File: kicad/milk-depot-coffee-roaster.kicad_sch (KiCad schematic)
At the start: 8 parts, among them J1 BT Thermocouple (35mm/2.5mm), J2 ET Thermocouple (50mm/3.0mm), J3 OLED 1.3in IIC, U1 MAX31855KASA, U2 MAX31855KASA

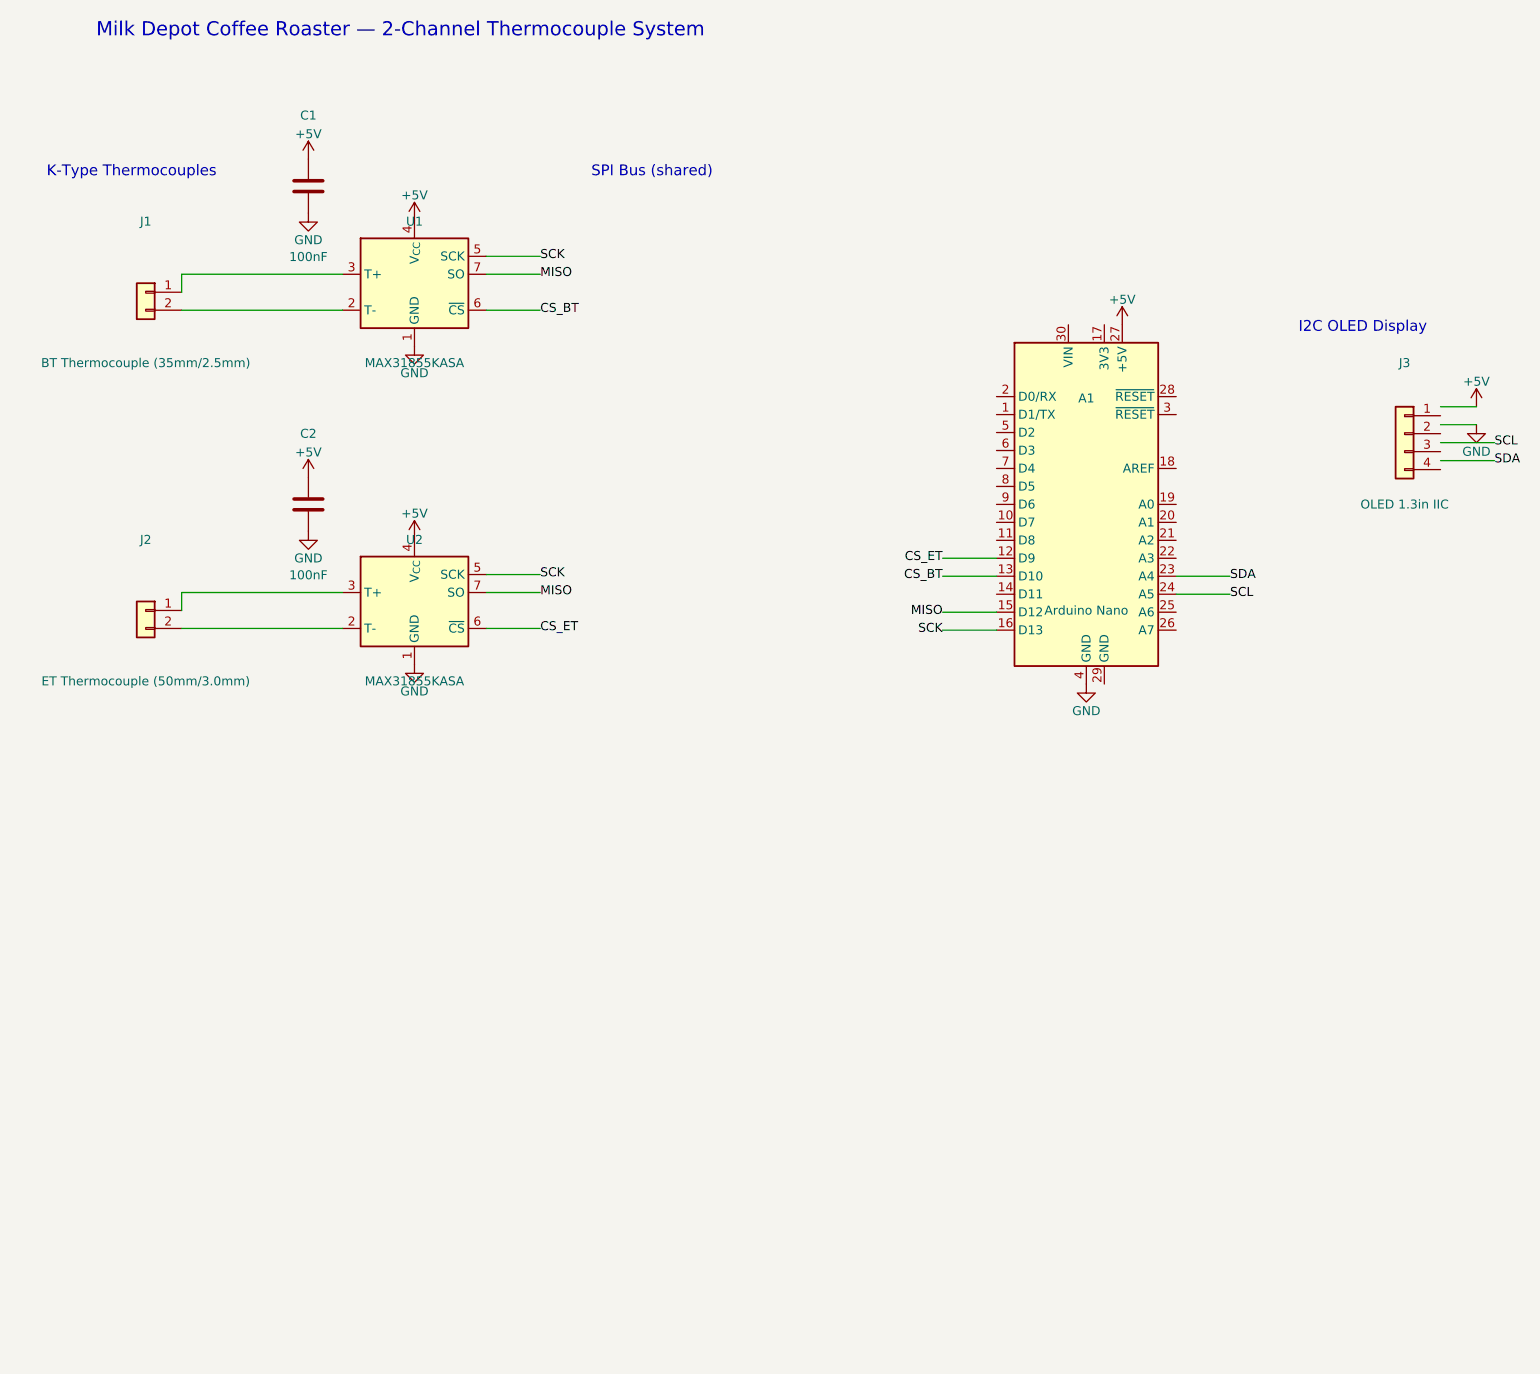
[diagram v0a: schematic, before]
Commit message: Scaffold new KiCad 10 project for ESP32 redesign
- Archive old Arduino Nano schematic to kicad/archive/v1-nano/
- New project with JLCPCB-compatible design rules (2-layer, A3 schematic)
- Place ESP32-WROOM-32E, 2× MAX31855KASA, 2× BSS138 symbols (validated against datasheets)
- Set up project-local symbol/footprint libraries and BOM fields (MPN, DigiKey_PN)
- Add component datasheets (ESP32, MAX31855, BSS138, LCD)
- Update .gitignore for KiCad 10 patterns
- Update RESUME.md and STATUS.md with procurement and schematic progress

Co-Authored-By: Claude Opus 4.6 (1M context) <noreply@anthropic.com>
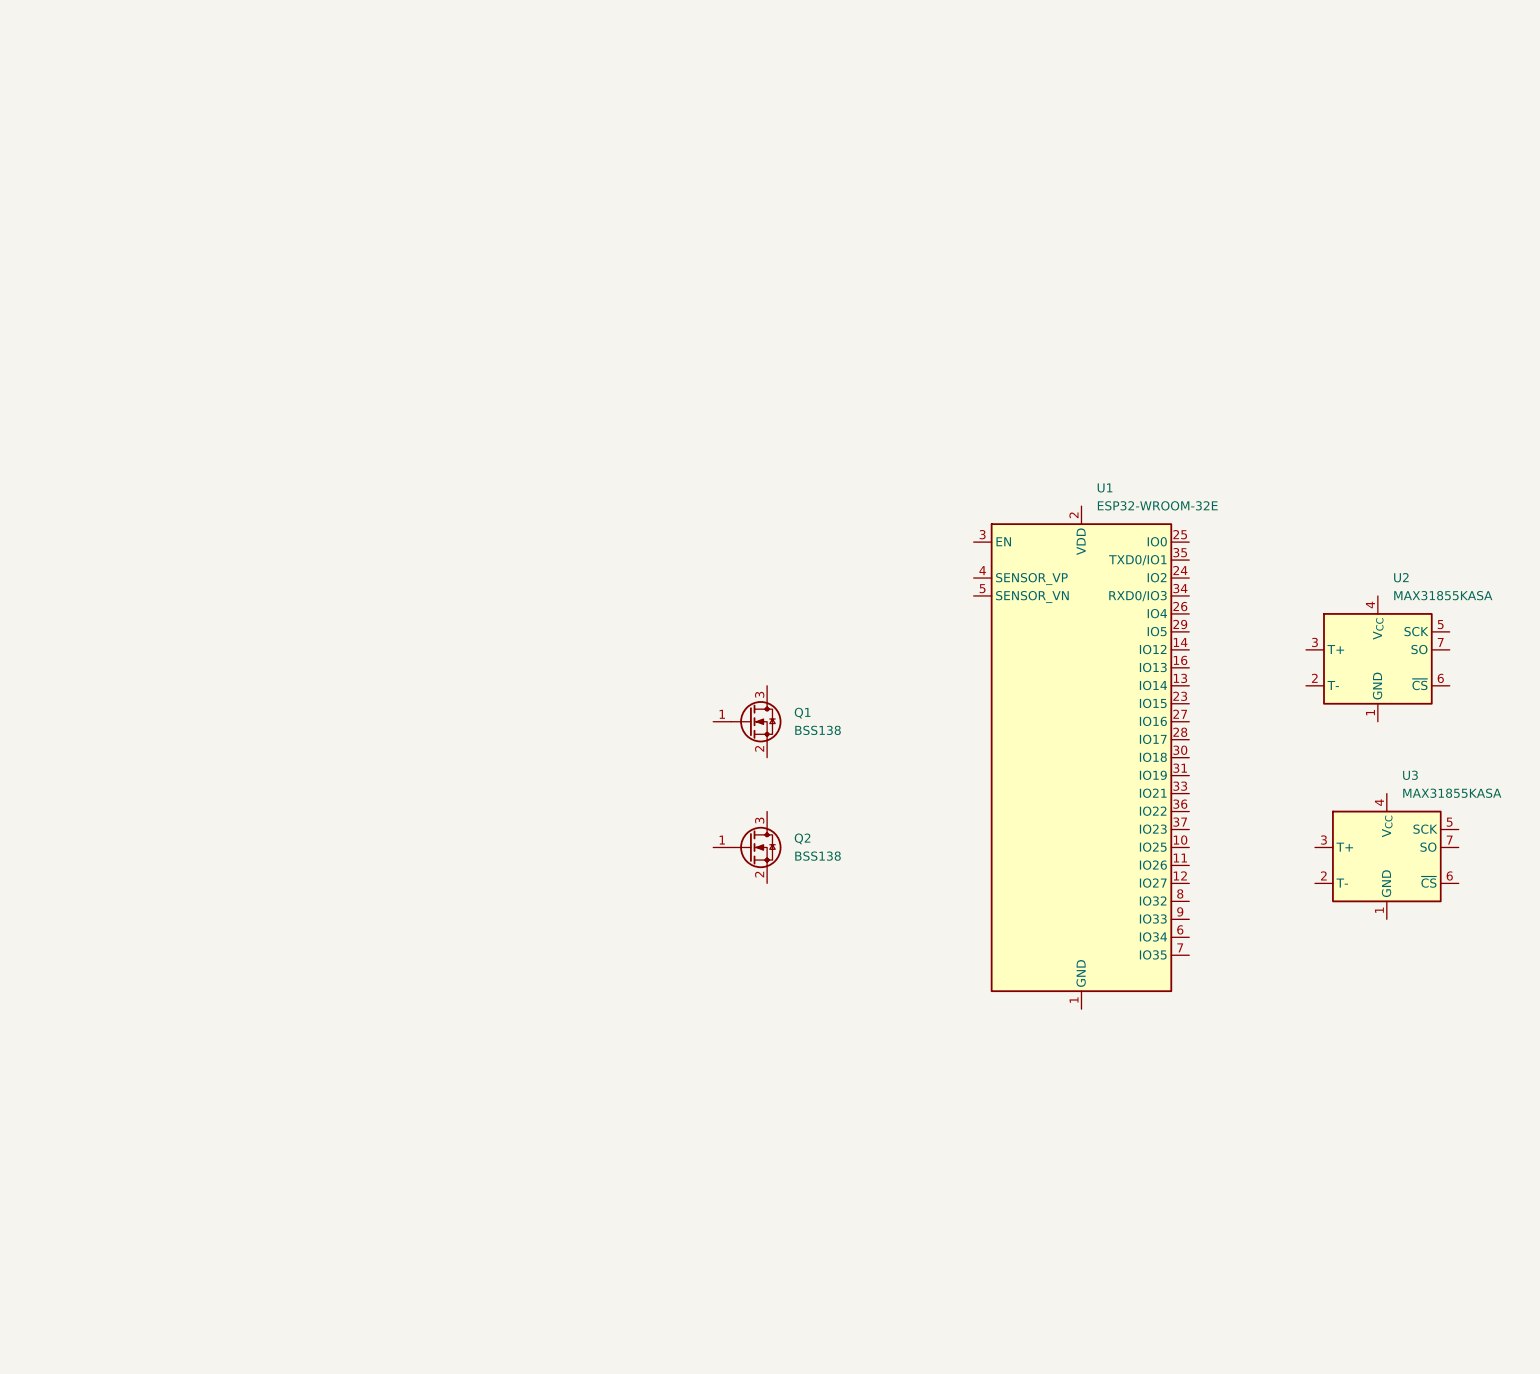
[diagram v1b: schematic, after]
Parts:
- removed A1: Arduino Nano, symbol MCU_Module:Arduino_Nano_v2.x
- removed C1, C2: 100nF, symbol Device:C
- removed J1: BT Thermocouple (35mm/2.5mm), symbol Connector_Generic:Conn_01x02
- removed J2: ET Thermocouple (50mm/3.0mm), symbol Connector_Generic:Conn_01x02
- removed J3: OLED 1.3in IIC, symbol Connector_Generic:Conn_01x04
- removed U1: MAX31855KASA, symbol Sensor_Temperature:MAX31855KASA
- added Q1, Q2: BSS138, Package_TO_SOT_SMD:SOT-23, symbol Transistor_FET:BSS138
- added U1: ESP32-WROOM-32E, RF_Module:ESP32-WROOM-32E, symbol RF_Module:ESP32-WROOM-32E
- added U3: MAX31855KASA, Package_SO:SOIC-8_3.9x4.9mm_P1.27mm, symbol Sensor_Temperature:MAX31855KASA
- U2: footprint (none) -> Package_SO:SOIC-8_3.9x4.9mm_P1.27mm; DigiKey_PN (none) -> MAX31855KASA+-ND; MPN (none) -> MAX31855KASA+; Manufacturer (none) -> Analog Devices
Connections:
- net +5V: no longer names the net of U2.4 (V_{CC})
- net CS_ET: no longer names the net of U2.6 (~{CS})
- net GND: no longer names the net of U2.1 (GND)
- net MISO: no longer names the net of U2.7 (SO)
- net SCK: no longer names the net of U2.5 (SCK)
- new net: U1.1 (GND), U1.15 (GND), U1.38 (GND), U1.39 (GND)
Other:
- note removed: "I2C OLED Display"
- note removed: "K-Type Thermocouples"
- note removed: "Milk Depot Coffee Roaster — 2-Channel Thermocouple System"
- note removed: "SPI Bus (shared)"
- title: Milk Depot Coffee Roaster - 2-Channel Thermocouple System -> Milk Depot Coffee Roaster — Temperature Controller

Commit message: Verify procurement and add component datasheets for schematic capture
- Audit all supplier invoices, correct stale BOM references (DK #122017091 was fully returned)
- Download datasheets for NCP1117, MMBT2222A, TL3342, OSTTC020162, DG127, B4B-PH-K-S, caps
- Place R1-R6 and C1 with BOM fields (MPN, Manufacturer, DigiKey_PN)
- Remove old generate_schematic.py (was for archived Nano schematic)
- Update RESUME.md and STATUS.md with verified procurement status

Co-Authored-By: Claude Opus 4.6 <noreply@anthropic.com>
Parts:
- added C1, C2, C3, C8: 100nF, Capacitor_SMD:C_0805_2012Metric, symbol Device:C
- added C4, C5: 10nF, Capacitor_SMD:C_0805_2012Metric, symbol Device:C
- added C6, C7: 1µF, Capacitor_SMD:C_0805_2012Metric, symbol Device:C
- added C9: 10µF, Capacitor_SMD:C_0805_2012Metric, symbol Device:C
- added J1: Conn_01x02, symbol Connector_Generic:Conn_01x02
- added Q3, Q4: MMBT2222A, Package_TO_SOT_SMD:SOT-23, symbol Transistor_BJT:MMBT2222A
- added R1, R2, R3, R4, R5, R6: 10k, Resistor_SMD:R_0805_2012Metric, symbol Device:R
- added U4: NCP1117-3.3_SOT223, Package_TO_SOT_SMD:SOT-223-3_TabPin2, symbol Regulator_Linear:NCP1117-3.3_SOT223
